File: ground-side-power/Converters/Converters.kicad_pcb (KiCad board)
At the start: 2 copper layers, 82.8 x 74.4 mm, 51 parts, among them J1 DAQ Voltage Sensing, J2 DAQ Current Sensing, J3 Ground Connections, J4 BATT_IN, J5 POWER_OUT, J6 5V_IN, U1 K7805-3AR3, U2 TPS55340, U3 INA180, U4 INA180

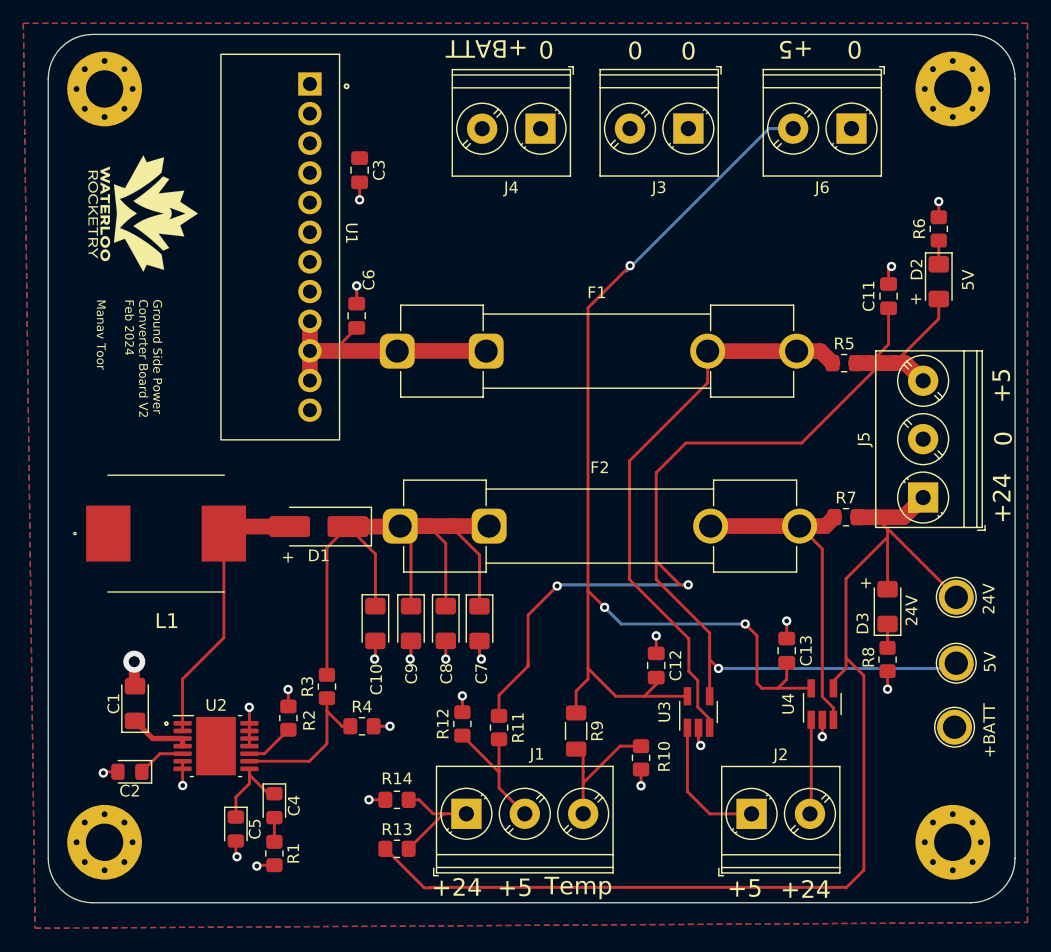
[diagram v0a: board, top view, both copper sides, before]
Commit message: fixed drc errors and changed thermistor symbol
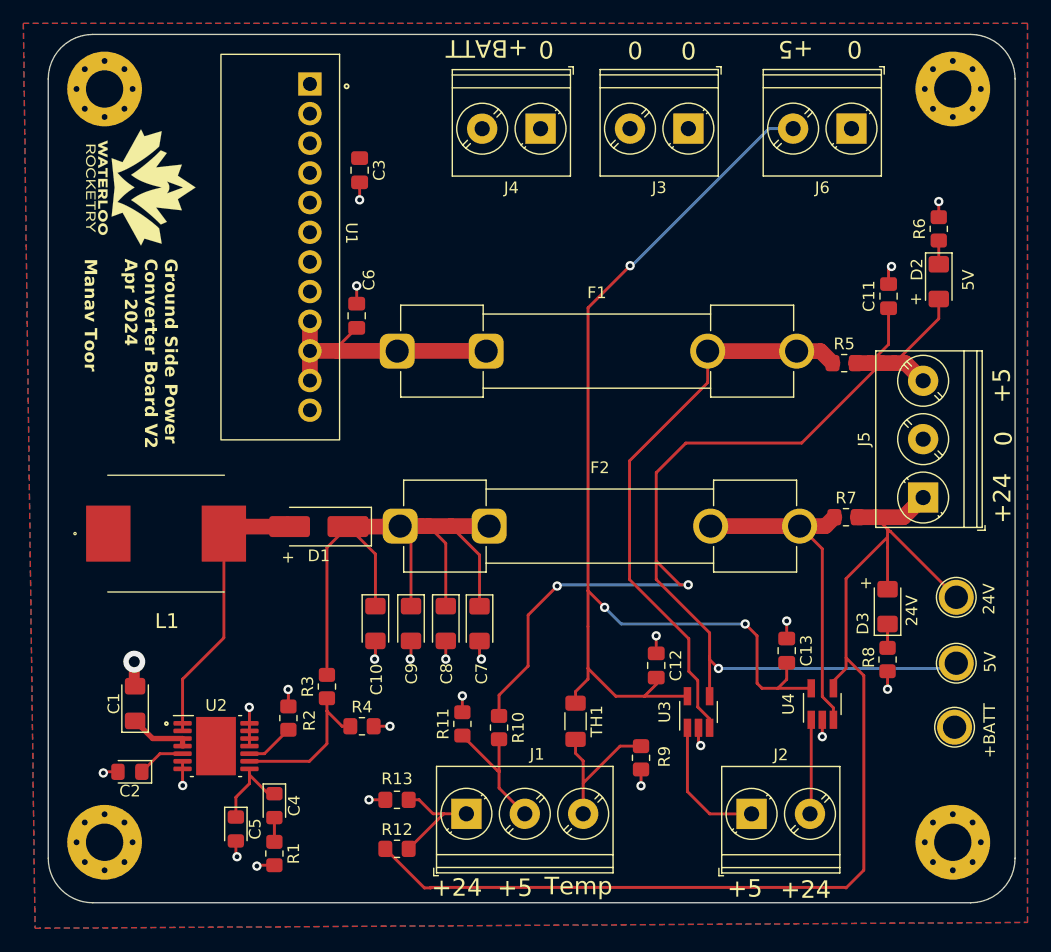
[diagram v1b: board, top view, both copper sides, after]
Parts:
- removed the R9 at (148.8, 126.1)
- added TH1: B57621C5103K062, Resistor_SMD:R_1206_3216Metric_Pad1.30x1.75mm_HandSolder, F.Cu at (148.8, 125.3)
- moved G*** 2.24 mm to (111.6, 79.6)
- renumbered R11 to R10, R12 to R11, R13 to R12, R14 to R13, R10 to R9
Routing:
- net +5V: track 212.1 -> 210.4 mm
- net /Temp: track 12.1 -> 12.9 mm
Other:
- board text added: "Ground Side Power Converter Board V2 Apr 2024 Manav Toor"
- board text removed: "Ground Side Power Converter Board V2 Feb 2024 Manav Toor"

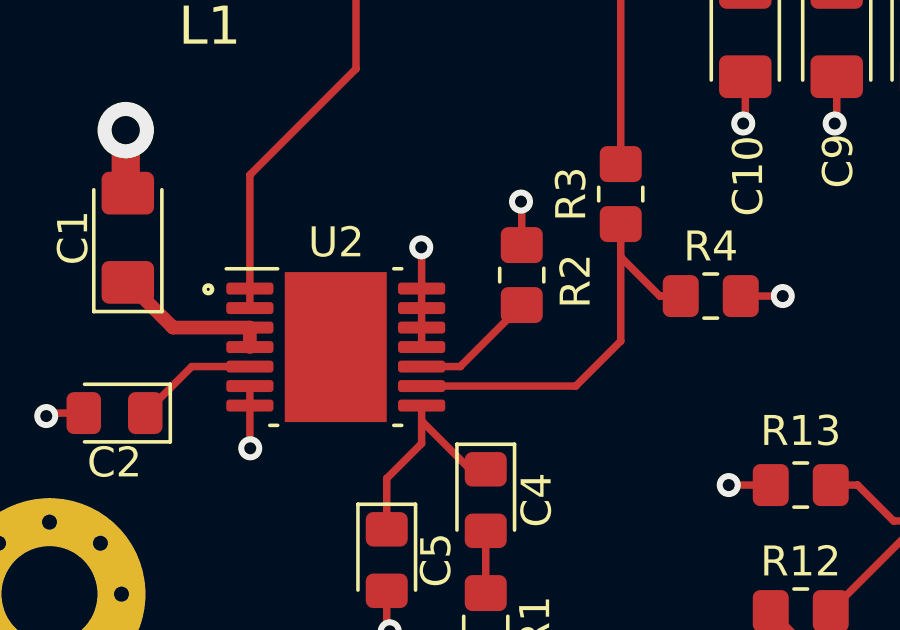
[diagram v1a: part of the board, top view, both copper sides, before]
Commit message: removed daisychaining
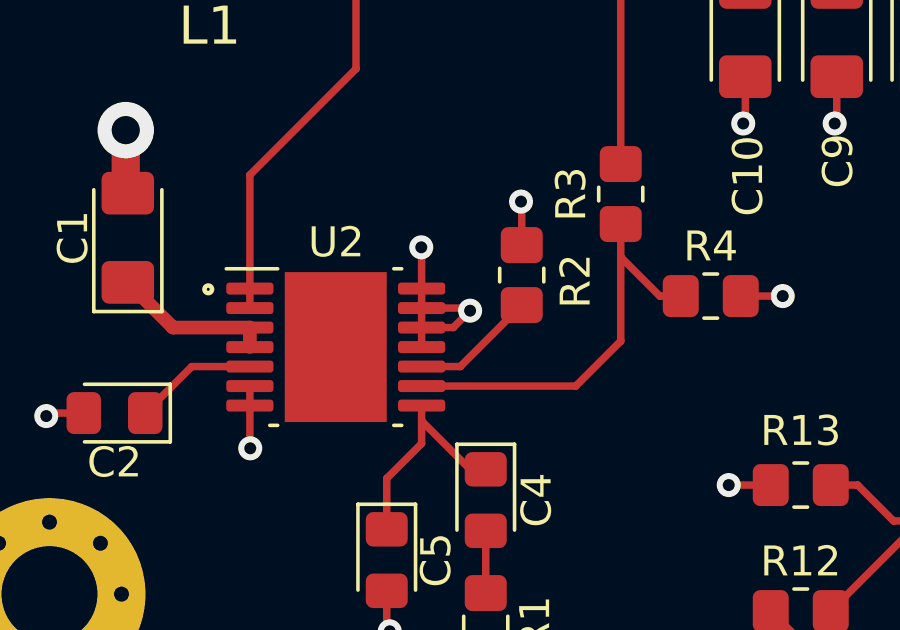
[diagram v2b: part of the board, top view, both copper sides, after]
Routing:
- net GND: track 38.7 -> 42.2 mm, vias 24 -> 25
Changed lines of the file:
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@@
     (effects (font (size 1.5 1.5) (thickness 0.3)))
   )
+  (segment (start 122.4788 126.1872) (end 121.916 126.75) (width 0.25) (layer "F.Cu") (net 1))
   (segment (start 108.45 129.6) (end 108.35 129.7) (width 0.25) (layer "F.Cu") (net 1))
   (segment (start 119.7 136.775) (end 119.8 136.875) (width 0.25) (layer "F.Cu") (net 1))
@@
   (segment (start 132.5 132) (end 131.1 132) (width 0.25) (layer "F.Cu") (net 1))
   (segment (start 121.575 137.6) (end 121.5 137.675) (width 0.25) (layer "F.Cu") (net 1))
+  (segment (start 120.8625 126.1) (end 122.3916 126.1) (width 0.25) (layer "F.Cu") (net 1))
+  (segment (start 121.916 126.75) (end 120.8625 126.75) (width 0.25) (layer "F.Cu") (net 1))
   (segment (start 175.6 86.5765) (end 175.854 86.3225) (width 0.25) (layer "F.Cu") (net 1))
   (segment (start 154.4 129.4) (end 154.4 130.8) (width 0.25) (layer "F.Cu") (net 1))
@@
   (segment (start 123 137.6) (end 121.575 137.6) (width 0.25) (layer "F.Cu") (net 1))
   (segment (start 134.7 119.879) (end 134.631 119.948) (width 0.25) (layer "F.Cu") (net 1))
+  (segment (start 122.3916 126.1) (end 122.4788 126.1872) (width 0.25) (layer "F.Cu") (net 1))
   (segment (start 119.7 135.525) (end 119.7 136.775) (width 0.25) (layer "F.Cu") (net 1))
   (segment (start 139.1 124.5) (end 139.1 123.1) (width 0.25) (layer "F.Cu") (net 1))
@@
   (via (at 137.679 119.948) (size 0.8) (drill 0.4) (layers "F.Cu" "B.Cu") (free) (net 1))
   (via (at 179.9 80.7615) (size 0.8) (drill 0.4) (layers "F.Cu" "B.Cu") (free) (net 1))
+  (via (at 122.4788 126.1872) (size 0.8) (drill 0.4) (layers "F.Cu" "B.Cu") (free) (net 1))
   (via (at 159.512 127.353923) (size 0.8) (drill 0.4) (layers "F.Cu" "B.Cu") (free) (net 1))
   (via (at 131.583 119.948) (size 0.8) (drill 0.4) (layers "F.Cu" "B.Cu") (free) (net 1))

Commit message: generated gerbers and sch pdf
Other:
- board text added: "JLCJLCJLCJLC"
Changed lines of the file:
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@@
     (effects (font (size 1.0682 1.0682) (thickness 0.1778) bold) (justify left bottom))
+  )
+  (gr_text "JLCJLCJLCJLC" (at 124.0028 92.1004 90) (layer "F.SilkS")
+    (effects (font (size 1.5 1.5) (thickness 0.3) bold) (justify left bottom))
   )
   (gr_text "5V" (at 182.43 87.483577 90) (layer "F.SilkS")

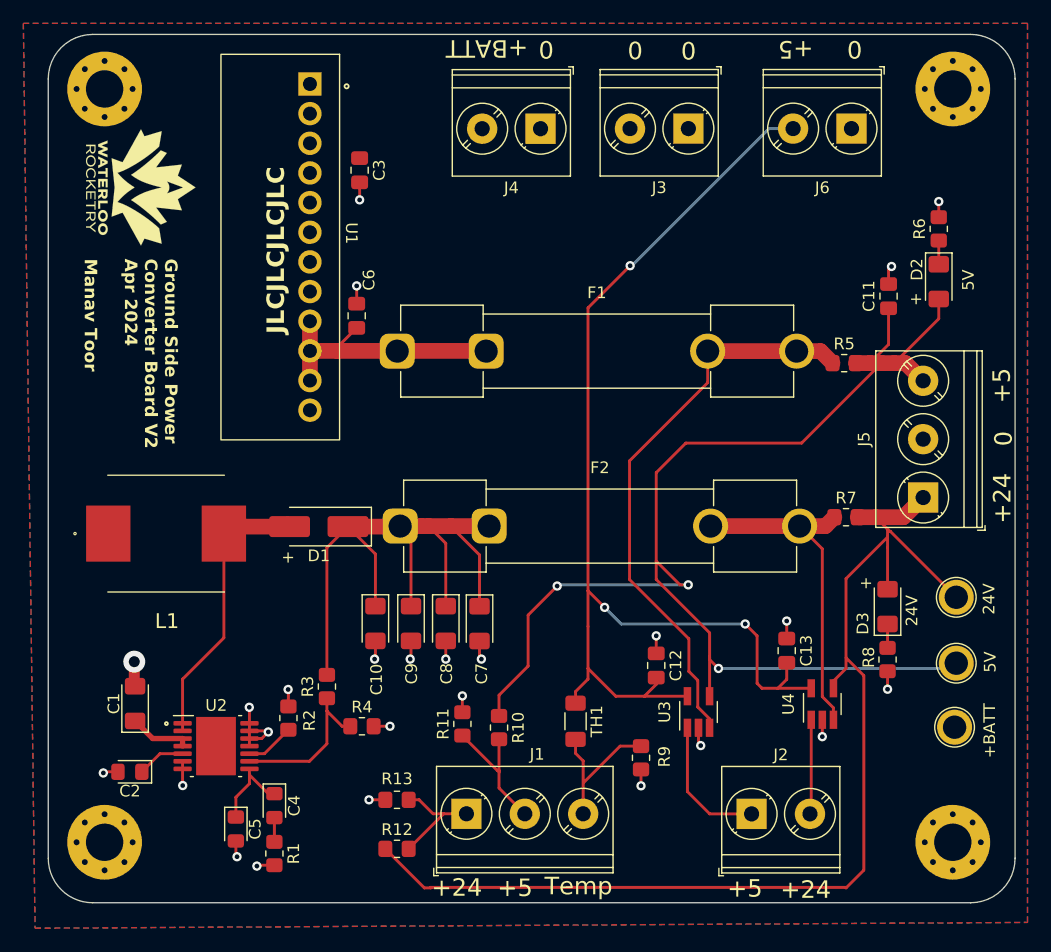
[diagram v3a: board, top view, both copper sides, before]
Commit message: add pours near boost converter and new gerbers
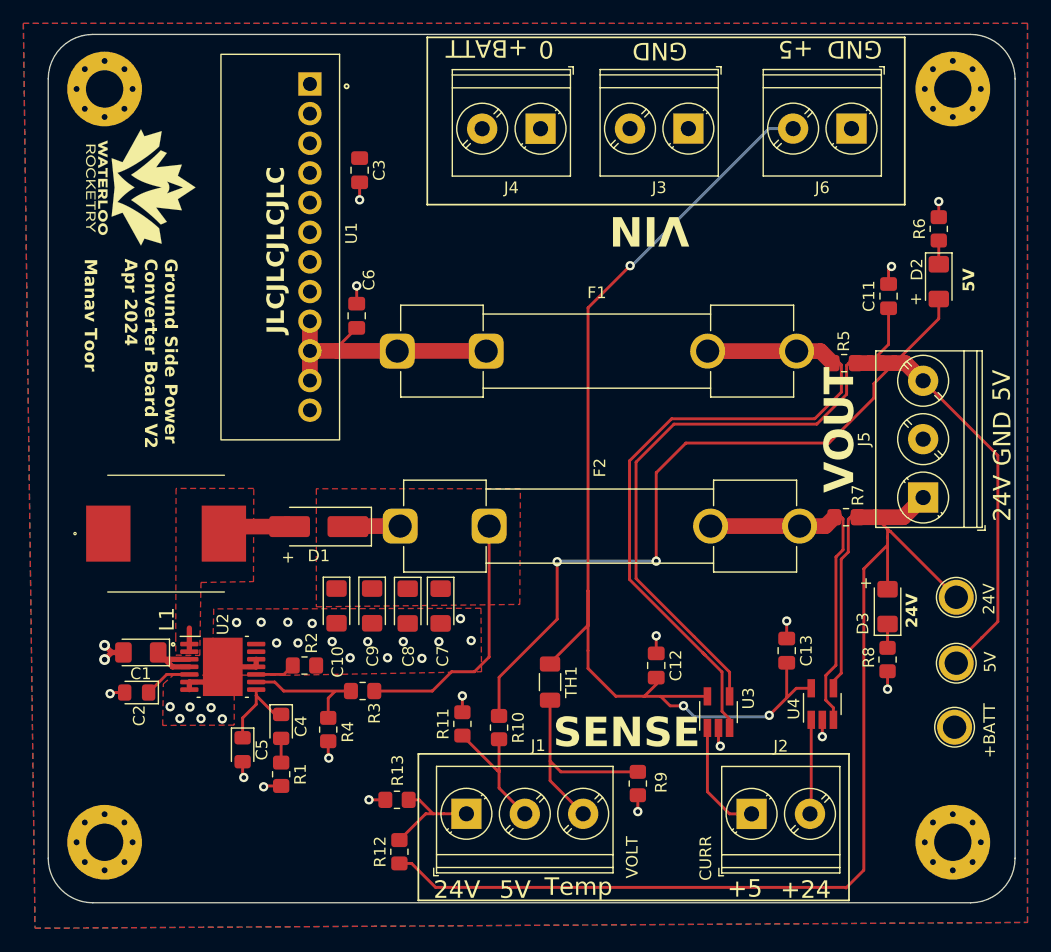
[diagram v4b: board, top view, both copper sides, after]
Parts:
- moved C4 6.81 mm to (123.6, 125.7)
- moved C5 6.81 mm to (120.3, 127.7)
- moved R1 6.81 mm to (123.6, 129.8)
- moved U2 6.81 mm to (118.6, 120.6)
- moved C2 6.81 mm to (111.2, 122.8)
- moved R2 4.71 mm to (125.6, 120.5), turned to 0 degrees
- moved C1 4.40 mm to (111.6, 119.4), turned to 180 degrees
- moved TH1 4.00 mm to (146.6, 121.9)
- moved C7 3.66 mm to (137.2, 115.4)
- moved C10 3.66 mm to (128.3, 115.4)
- moved C9 3.66 mm to (131.4, 115.4)
- moved C8 3.59 mm to (134.4, 115.4)
- moved R3 3.08 mm to (130.6, 122.7), turned to 0 degrees
- moved R4 2.90 mm to (127.6, 126.0), turned to -90 degrees
- moved R9 2.22 mm to (154.1, 130.6)
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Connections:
- U2 pad : (no net) -> GND
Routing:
- net +5V: track 210.4 -> 244.7 mm, vias 6 -> 5
- net Net-(D1-K): track 57.2 -> 28.1 mm
- net Net-(D1-A): track 24.5 -> 8.17 mm
- net /5V_Sense+: track 49.0 -> 61.6 mm
- net +24V: track 98.1 -> 107.1 mm
- net GND: track 42.2 -> 34.2 mm, vias 25 -> 39
- net /Temp: track 12.9 -> 18.8 mm
- net Net-(U2-FB): track 13.7 -> 10.9 mm
- net /5V_OUT: track 11.8 -> 10.0 mm
- net /24V_Sense+: track 28.7 -> 30.2 mm
- net +BATT: track 5.34 -> 6.10 mm
- net Net-(U2-FREQ): track 4.19 -> 3.45 mm
- added copper zone on F.Cu, net GND
- added copper zone on F.Cu, net Net-(D1-A)
- added copper zone on F.Cu, net Net-(D1-K)
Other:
- board text added: "CURR"
- board text added: "GND"
- board text added: "SENSE"
- board text added: "VIN"
- board text added: "VOLT"
- board text added: "VOUT"

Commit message: connected 5v traces
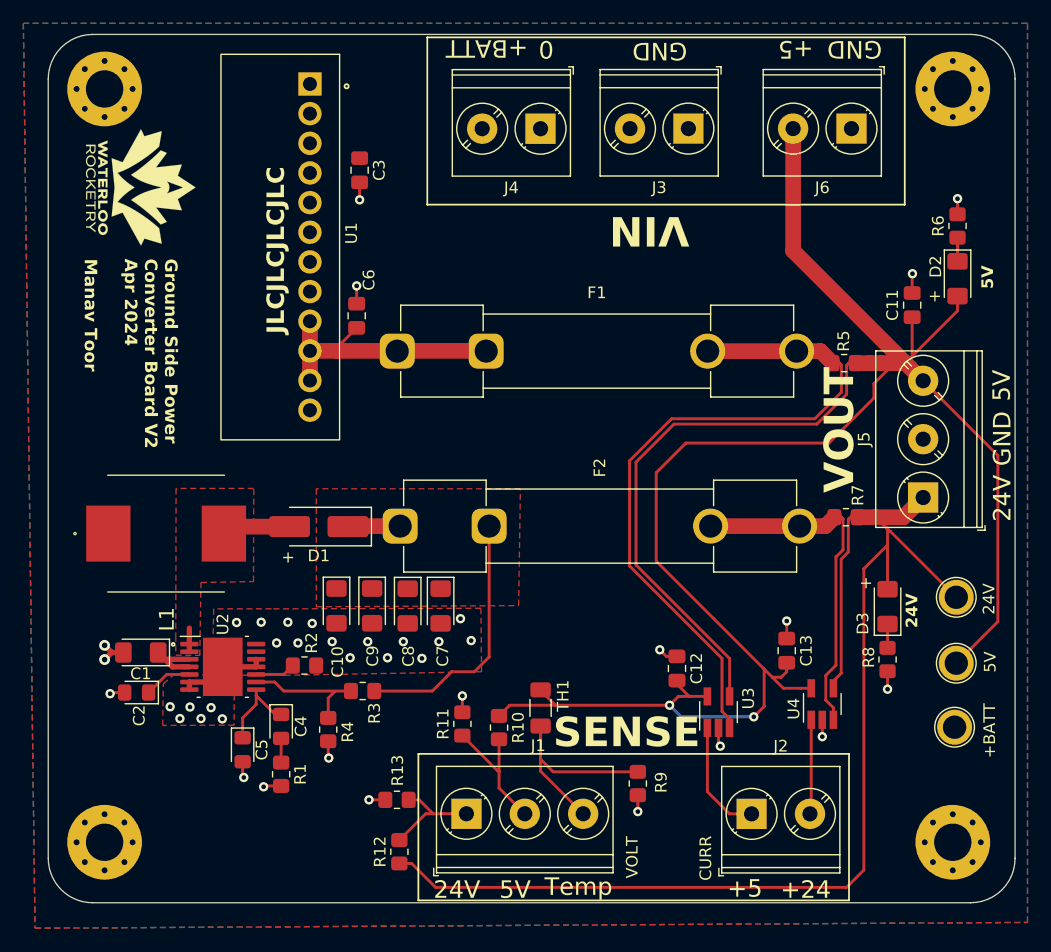
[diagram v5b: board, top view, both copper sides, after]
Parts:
- moved TH1 2.35 mm to (145.8, 124.1)
- moved C11 2.16 mm to (177.6, 89.6)
- moved C12 1.80 mm to (157.5, 120.8)
- moved D2 1.63 mm to (181.5, 87.4)
- moved R6 1.63 mm to (181.5, 82.9)
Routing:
- net +5V: track 244.7 -> 203.8 mm, vias 5 -> 2
- net /Temp: track 18.8 -> 17.8 mm
